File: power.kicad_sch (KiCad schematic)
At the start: 45 parts, among them U5 MIC5504-3.3YM5-TR

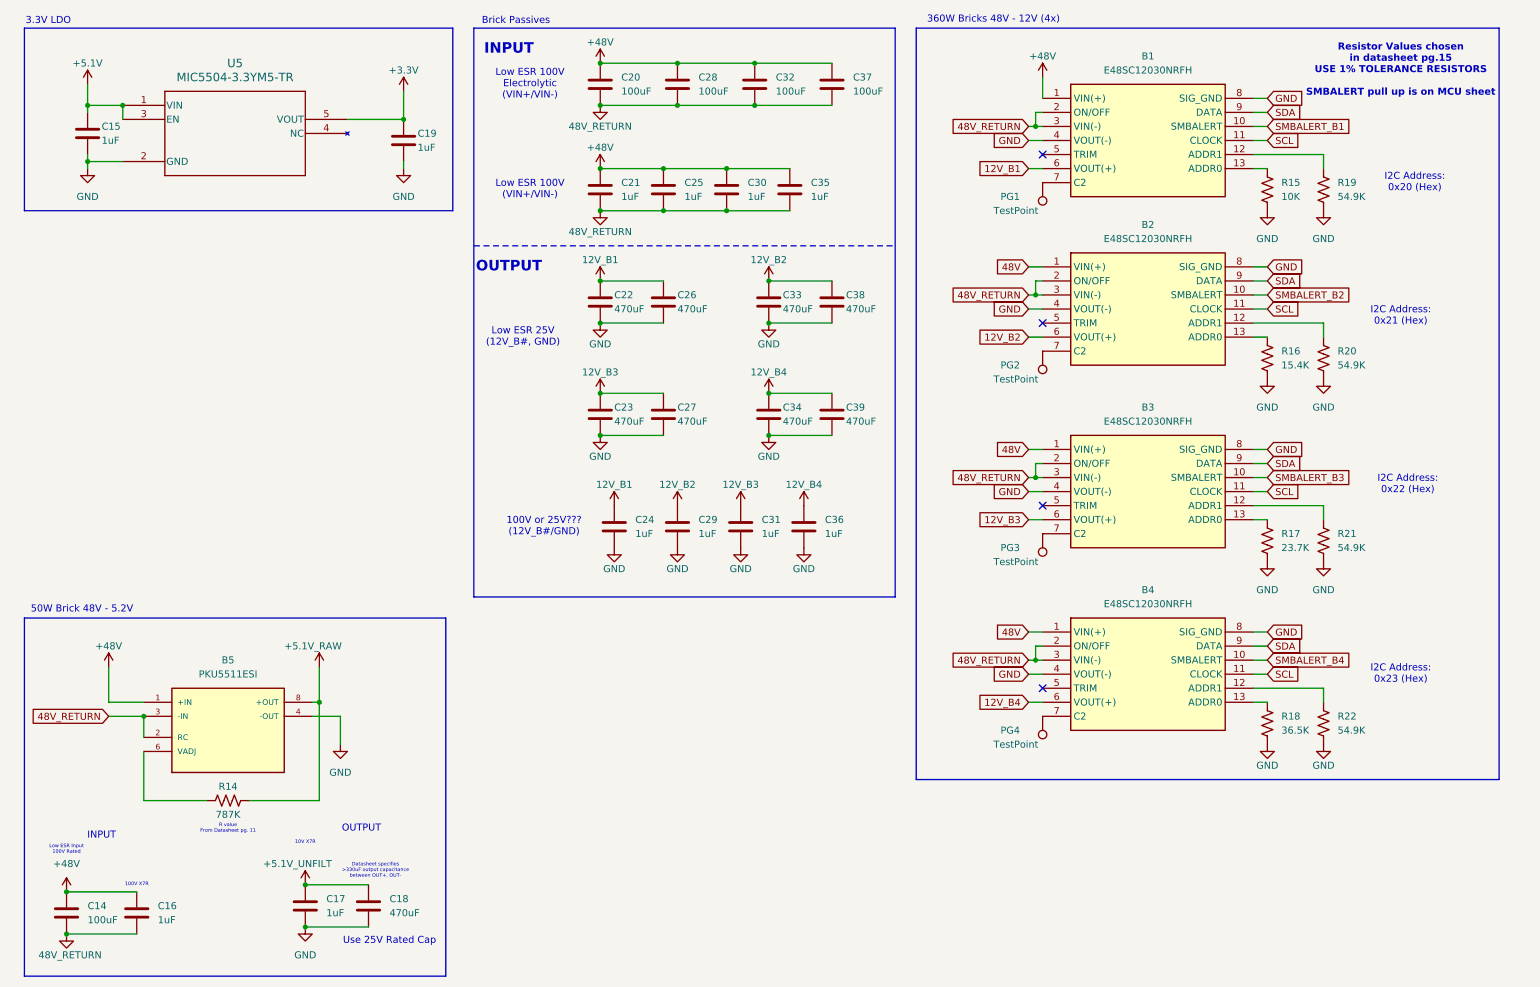
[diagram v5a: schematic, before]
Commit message: Prettified, more power changes and MCU pin changes and removing redundancies
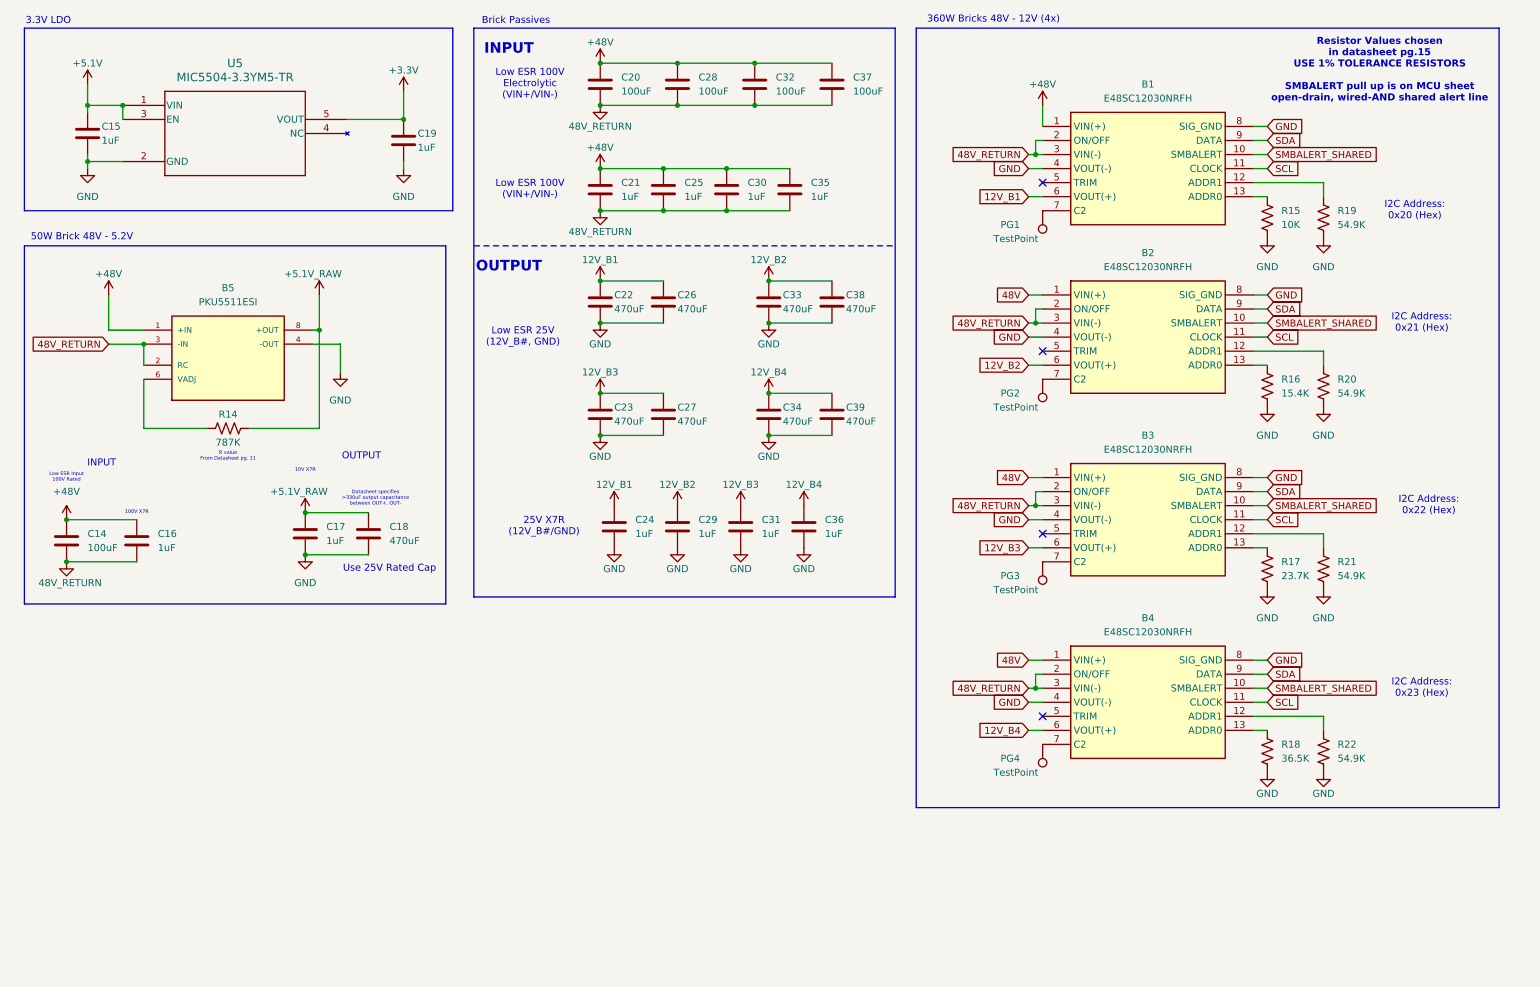
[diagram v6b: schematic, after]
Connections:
- net +5.1V_UNFILT is gone; now on net +5.1V_RAW: C17.1, C18.1
- net SMBALERT_B2 is gone; now on net SMBALERT_SHARED: B2.10 (SMBALERT)
- net SMBALERT_B3 is gone; now on net SMBALERT_SHARED: B3.10 (SMBALERT)
- net SMBALERT_B4 is gone; now on net SMBALERT_SHARED: B4.10 (SMBALERT)
- net SMBALERT_B1 renamed SMBALERT_SHARED
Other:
- note added: "25V X7R (12V_B#/GND)"
- note added: "Resistor Values chosen in datasheet pg.15 USE 1% TOLERANCE RESISTORS SMBALERT pull up is on MCU sheet open-drain, wired-AND shared alert line"
- note removed: "100V or 25V??? (12V_B#/GND)"
- note removed: "Resistor Values chosen in datasheet pg.15 USE 1% TOLERANCE RESISTORS SMBALERT pull up is on MCU sheet"
- moved on the sheet: B1, B2, B3, B4, B5, C14, C16, C17, C18, PG1, PG2, PG3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

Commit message: Replaced improper brick with new one
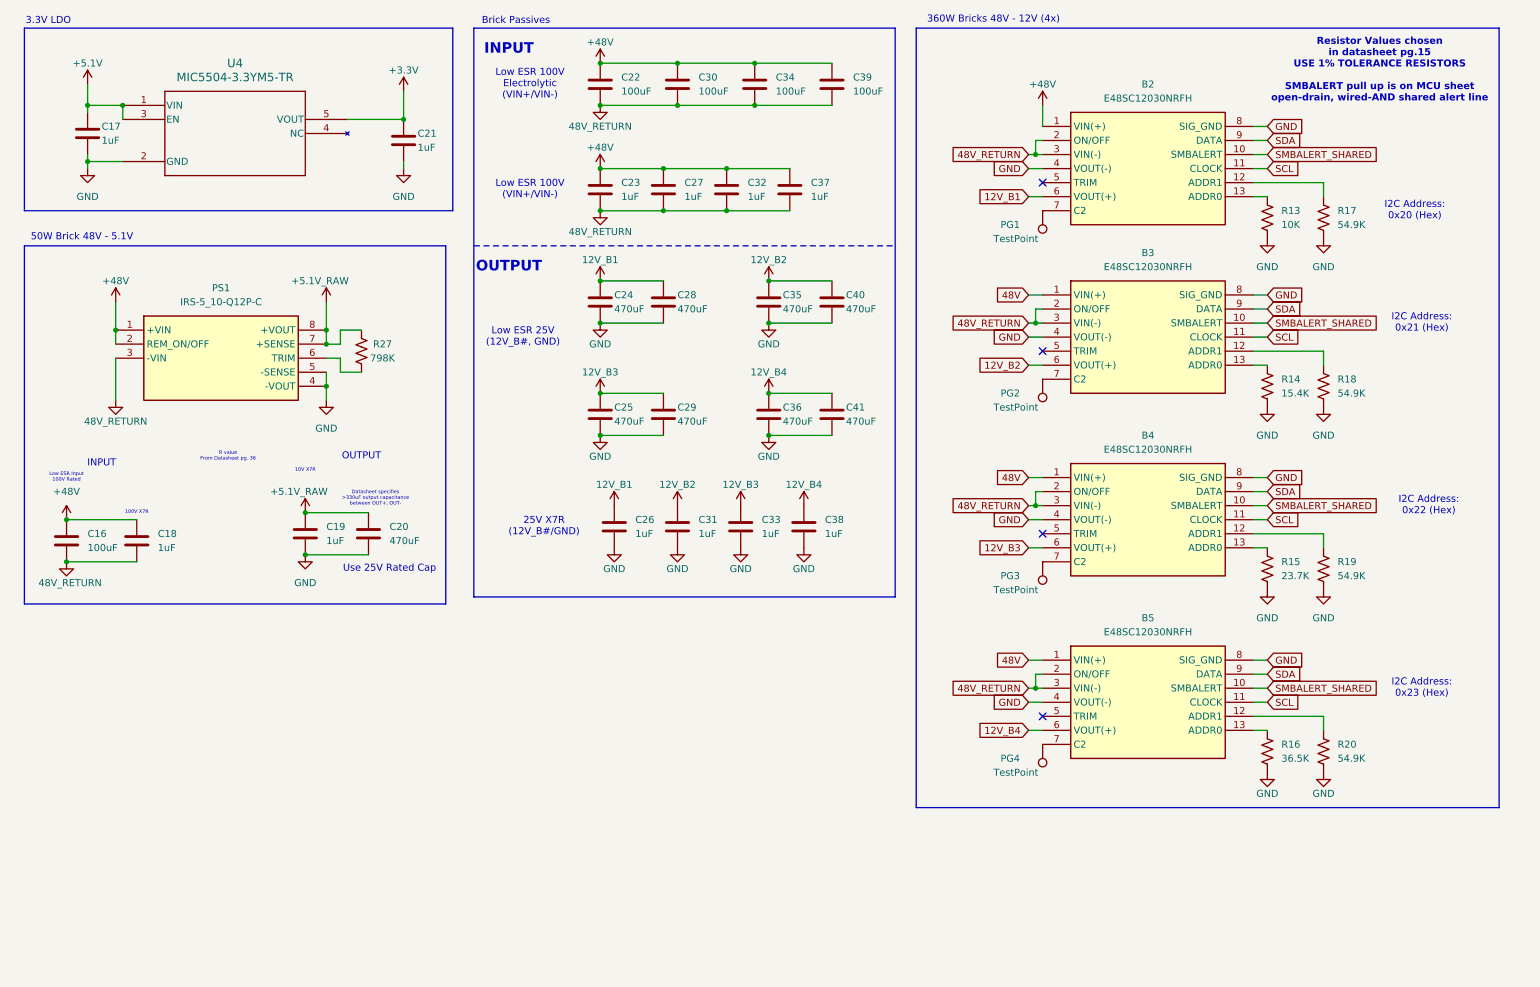
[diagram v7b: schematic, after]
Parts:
- removed B5: PKU5511ESI, PKU5511ESI:CONV_PKU5511ESI, symbol PKU5511ESI:PKU5511ESI
- removed R14: 787K, symbol Device:R_US
- added PS1: IRS-5_10-Q12P-C, IRS510Q12PC, symbol IRS-5_10-Q12P-C:IRS-5_10-Q12P-C
- added R27: 798K, symbol Device:R_US
- renumbered B1 to B2, B2 to B3, B3 to B4, B4 to B5, C14 to C16, C15 to C17, C16 to C18, C17 to C19, C18 to C20, C19 to C21, C20 to C22, C21 to C23, C22 to C24, C23 to C25, C24 to C26, C25 to C27, C26 to C28, C27 to C29, C28 to C30, C29 to C31, C30 to C32, C31 to C33, C32 to C34, C33 to C35, C34 to C36, C35 to C37, C36 to C38, C37 to C39, C38 to C40, C39 to C41, R15 to R13, R16 to R14, R17 to R15, R18 to R16, R19 to R17, R20 to R18, R21 to R19, R22 to R20, U5 to U4
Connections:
- net +48V: now also PS1.1 (+VIN), PS1.2 (REM_ON/OFF)
- net +5.1V_RAW: now also PS1.7 (+SENSE), PS1.8 (+VOUT), R27.2
- net 48V_RETURN: now also PS1.3 (-VIN)
- net GND: now also PS1.4 (-VOUT), PS1.5 (-SENSE)
- new net: PS1.6 (TRIM), R27.1
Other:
- note added: "50W Brick 48V - 5.1V"
- note added: "R value From Datasheet pg. 36"
- note removed: "50W Brick 48V - 5.2V"
- note removed: "R value From Datasheet pg. 11"

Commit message: Bennett TODOs
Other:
- note added: "BRICK SHOULD BE THIS I6A4W020A033V-003-R"
- note added: "CHECK CAPACITORS CHECK DATASHEET OF I6A TO SEE WHAT MINIMUM OUPTUT"
- note added: "Can drop down to 63V, ideally would be 100V keep 63V if its too big"
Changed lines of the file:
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@@
+		)
+	)
+	(text "CHECK CAPACITORS \nCHECK DATASHEET OF I6A\nTO SEE WHAT MINIMUM OUPTUT"
+		(exclude_from_sim no)
+		(at 53.34 133.35 0)
+		(effects
+			(font
+				(size 1.27 1.27)
+				(color 255 37 1 1)
+			)
 		)
 	)
@@
 	(text "Low ESR 25V \n(12V_B#, GND)"
 		(exclude_from_sim no)
-		(at 105.41 80.01 0)
+		(at 105.41 77.47 0)
 		(effects
 			(font
@@
 		)
 	)
+	(text "BRICK SHOULD BE THIS\nI6A4W020A033V-003-R"
+		(exclude_from_sim no)
+		(at 52.07 95.25 0)
+		(effects
+			(font
+				(size 1.27 1.27)
+				(color 255 5 28 1)
+			)
+		)
+	)
 	(text "Resistor Values chosen \nin datasheet pg.15\nUSE 1% TOLERANCE RESISTORS\n\nSMBALERT pull up is on MCU sheet\nopen-drain, wired-AND shared alert line"
 		(exclude_from_sim no)
@@
 			)
 		)
+	)
+	(text "Can drop down to 63V,\nideally would be 100V\nkeep 63V if its too big"
+		(exclude_from_sim no)
+		(at 147.32 44.45 0)
+		(effects
+			(font
+				(size 1.27 1.27)
+				(color 255 0 23 1)
+			)
+		)
